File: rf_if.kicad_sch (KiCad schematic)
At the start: 86 parts, among them IC1 SBL-1+, Q1 2N5109, Q2 J310, Q3 2N2219A, Q4 2N2219A, U2 Adafruit_Si5351, U3 74LVC74, U4 74HCT244, U5 74HC4066, U6 LM358, U7 74HC4066, U8 LM358

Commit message: AGC Work 2
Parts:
- added C162: 100nF, symbol Device:C_Small
- added C163: 10uF, symbol Device:C_Polarized_Small
- added R107: 47k/NoH, symbol Device:R_Small
- added R108: 33k/NoH, symbol Device:R_Small
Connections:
- net GND: now also U8.4 (V-), C162.2, C163.2, R108.1; no longer Q2.2 (S)
- net at U8.5 (IN2+): now also R107.1, R108.2
- net at U8.6 (IN2-): now also Q2.2 (S), U8.7 (OUT2), C162.1, C163.1
- net +5V_MAIN: now reaches U8.8 (V+)
- net +5V_MAIN: now also R107.2

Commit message: AGC Work 3
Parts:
- added C164: 10pF, symbol Device:C_Small
- added C165: 4.7uF, symbol Device:C_Polarized_Small
- added D19: 1N4148, Diode_THT:D_DO-35_SOD27_P7.62mm_Horizontal, symbol Diode:1N4148
- added R109: 1M/NoH, symbol Device:R_Small
- added U10, U9: 74HC4066, symbol omega:74HC4066
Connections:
- net GND: now also C165.2, R109.2
- net IF_70M_OUT: now also C164.1
- net at R105.1, U8.1 (OUT1): now also U8.2 (IN1-)
- net at U8.3 (IN1+): now also C165.1, D19.1 (K), R109.1
- new net: C164.2, D19.2 (A)

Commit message: AGC Work 4
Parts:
- added R110: 120K/NoH, symbol Device:R_Small
- added R111: 100K/NoH, symbol Device:R_Small
- added RV12: 100k, symbol Device:R_Potentiometer_Trim
- renumbered C164 to C33, C165 to C34, C33 to C35, C34 to C36, C162 to C37, C163 to C38, C35 to C39, C36 to C40, C37 to C41, C38 to C42, C39 to C43, C40 to C44, C41 to C45, C42 to C46, C43 to C47, C44 to C48, C45 to C49, C46 to C50, C47 to C51, C48 to C52, C49 to C53, C50 to C54, C51 to C55, C52 to C56, D19 to D9, R109 to R13, R106 to R14, R105 to R15, R13 to R16, R107 to R17, R108 to R18, R14 to R19, R15 to R20, R16 to R21, R17 to R22, R18 to R23, R19 to R24, R20 to R25, R21 to R26, R22 to R27, R23 to R28, R24 to R29, R25 to R30, R26 to R31, R27 to R32, R28 to R33, R29 to R34, R30 to R35, R31 to R36, R32 to R37, R33 to R38, R34 to R39, R35 to R40, R36 to R41, R37 to R42, R38 to R43, R39 to R44, R40 to R45, R41 to R46, R42 to R47, R43 to R48, U7 to U10, U9 to U2, U8 to U3, U10 to U4, U2 to U5, U3 to U6, U4 to U7, U5 to U8, U6 to U9
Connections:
- net GND: now also U2.2 (1Z), RV12.3
- net DET_AGC: now reaches C34.1, D9.1 (K), R13.1
- net DET_AGC: now also U2.4 (2Y), R110.1; no longer U3.3 (IN1+)
- net DECAY_SSB: now reaches U2.1 (1Y)
- net DECAY_SSB: now also R110.2
- net AGC_SSB: now reaches U2.13 (1E)
- net AGC_SSB: now also U2.5 (2E)
- net THRESH_SSB: now reaches U2.3 (2Z)
- net THRESH_SSB: now also R111.1
- new net V_AGC_CTRL: R111.2, RV12.1, RV12.2, U3.3 (IN1+)
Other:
- moved on the sheet: C34, R13, U2, U4

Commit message: AGC work, ssb and cw
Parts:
- added C166: 100nF, symbol Device:C_Small
- added R112: 33K/NoH, symbol Device:R_Small
- added R113: 68K/NoH, symbol Device:R_Small
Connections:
- net +5V_MAIN: now also U2.14 (VCC), C166.1
- net DET_AGC: now also U2.11 (4Y), R112.1
- net GND: now also U2.7 (GND), U2.9 (3Z), C166.2
- net V_AGC_CTRL: now also R113.2
- net THRESH_CW: now reaches U2.10 (4Z)
- net THRESH_CW: now also R113.1
- net AGC_CW: now reaches U2.12 (4E)
- net AGC_CW: now also U2.6 (3E)
- net DECAY_CW: now reaches U2.8 (3Y)
- net DECAY_CW: now also R112.2
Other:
- moved on the sheet: RV12

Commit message: All AGCs done
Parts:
- added C45: 100nF, symbol Device:C_Small
- added R11, R25: 470K/NoH, symbol Device:R_Small
- added R22: 150K/NoH, symbol Device:R_Small
- added R9: 3M/NoH, symbol Device:R_Small
- renumbered C166 to C36, C36 to C37, C37 to C38, C38 to C39, C39 to C40, C40 to C41, C41 to C42, C42 to C43, C43 to C44, C44 to C46, C45 to C47, C46 to C48, C47 to C49, C48 to C50, C49 to C51, C50 to C52, C51 to C53, C52 to C54, C53 to C55, C54 to C56, C55 to C57, C56 to C58, R9 to R10, R112 to R12, R10 to R13, R11 to R14, R110 to R15, R12 to R16, R13 to R17, R14 to R18, R15 to R19, R111 to R20, R113 to R21, R16 to R23, R17 to R24, R18 to R26, R19 to R27, R20 to R28, R21 to R29, R22 to R30, R23 to R31, R24 to R32, R25 to R33, R26 to R34, R27 to R35, R28 to R36, R29 to R37, R30 to R38, R31 to R39, R32 to R40, R33 to R41, R34 to R42, R35 to R43, R36 to R44, R37 to R45, R38 to R46, R39 to R47, R40 to R48, R41 to R49, R42 to R50, R43 to R51, R44 to R52, R45 to R53, R46 to R54, R47 to R55, R48 to R56, RV12 to RV2
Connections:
- net +5V_MAIN: now also U4.14 (VCC), C45.1
- net DET_AGC: now also U4.11 (4Y), U4.4 (2Y), R11.1, R9.1
- net GND: now also U4.2 (1Z), U4.7 (GND), U4.9 (3Z), C45.2
- net V_AGC_CTRL: now also R22.2, R25.2
- net DECAY_AM: now reaches U4.1 (1Y)
- net DECAY_AM: now also R11.2
- net THRESH_DIG: now reaches U4.10 (4Z)
- net THRESH_DIG: now also R25.1
- net AGC_DIG: now reaches U4.12 (4E)
- net AGC_DIG: now also U4.6 (3E)
- net AGC_AM: now reaches U4.13 (1E)
- net AGC_AM: now also U4.5 (2E)
- net THRESH_AM: now reaches U4.3 (2Z)
- net THRESH_AM: now also R22.1
- net DECAY_DIG: now reaches U4.8 (3Y)
- net DECAY_DIG: now also R9.2
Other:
- moved on the sheet: C36, RV2, U2, U4

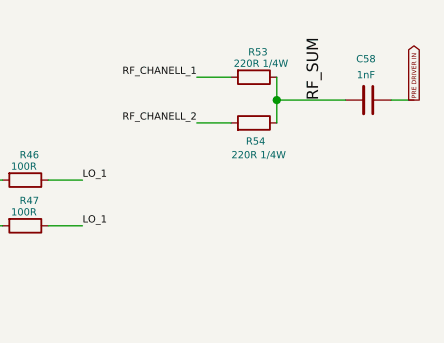
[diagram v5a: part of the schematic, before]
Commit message: Start of testing on LTspice
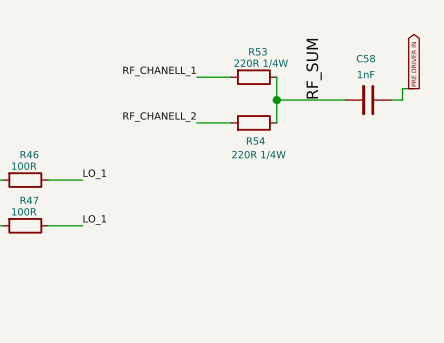
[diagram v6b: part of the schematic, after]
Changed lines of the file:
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@@
 	(wire
 		(pts
-			(xy 279.4 22.86) (xy 281.94 22.86)
+			(xy 280.67 21.59) (xy 281.94 21.59)
 		)
 		(stroke
@@
 	(wire
 		(pts
+			(xy 280.67 22.86) (xy 279.4 22.86)
+		)
+		(stroke
+			(width 0)
+			(type default)
+		)
+	)
+	(wire
+		(pts
 			(xy 213.36 134.62) (xy 215.9 134.62)
 		)
@@
 	(wire
 		(pts
+			(xy 280.67 21.59) (xy 280.67 22.86)
+		)
+		(stroke
+			(width 0)
+			(type default)
+		)
+	)
+	(wire
+		(pts
 			(xy 78.74 68.58) (xy 78.74 73.66)
 		)
@@
 	(global_label "PRE DRIVER IN"
 		(shape output)
-		(at 281.94 22.86 90)
+		(at 281.94 21.59 90)
 		(fields_autoplaced yes)
 		(effects
@@
 		)
 		(property "Intersheetrefs" "${INTERSHEET_REFS}"
-			(at 281.94 16.0893 90)
+			(at 281.94 14.8193 90)
 			(effects
 				(font
